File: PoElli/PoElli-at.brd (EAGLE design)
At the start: 100 x 80 mm, 142 parts, among them J1 DF12-ELLI-HEADER-TOP, J3 M022.54MM, J4 M022.54MM, Q1 SI1307DL, Q2 FDV301N, Q3 FDMC2674, Q4 IRFL4310, T1 Coilcraft 230NL, T2 FLYBACK750311689, U2 NCP1117, U3 FST3257, U4 LT3748, U5 TPS2378, U6 ENC424J600, X1 M-BOLT-2, X2 M-BOLT-2, X3 M-BOLT-2, X4 M-BOLT-2, Y1 25 MHz

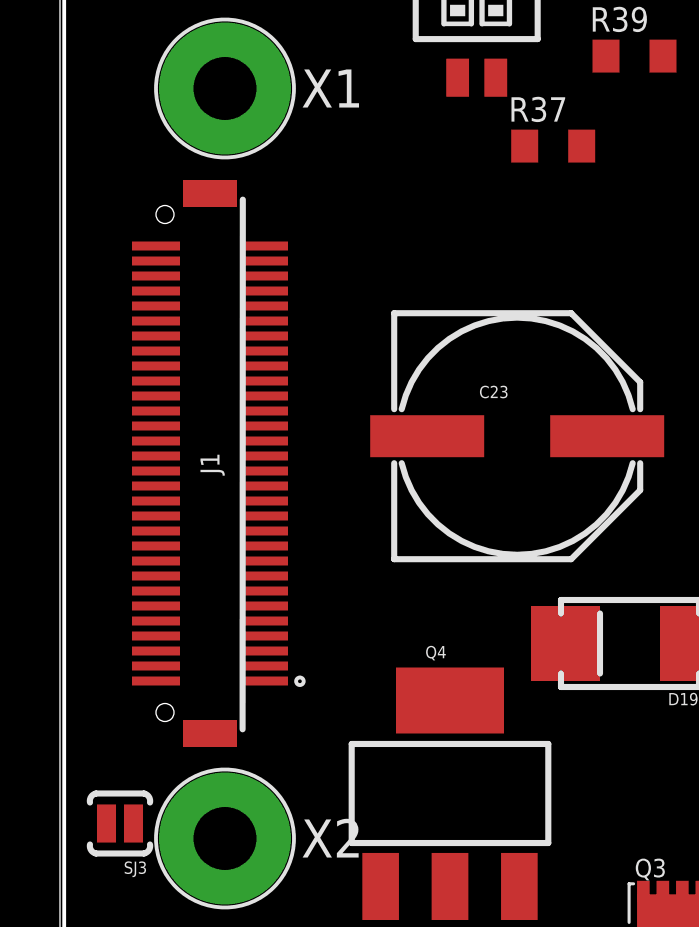
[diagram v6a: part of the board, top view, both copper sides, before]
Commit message: Move Hirose DF12 locations as agreed yesterday
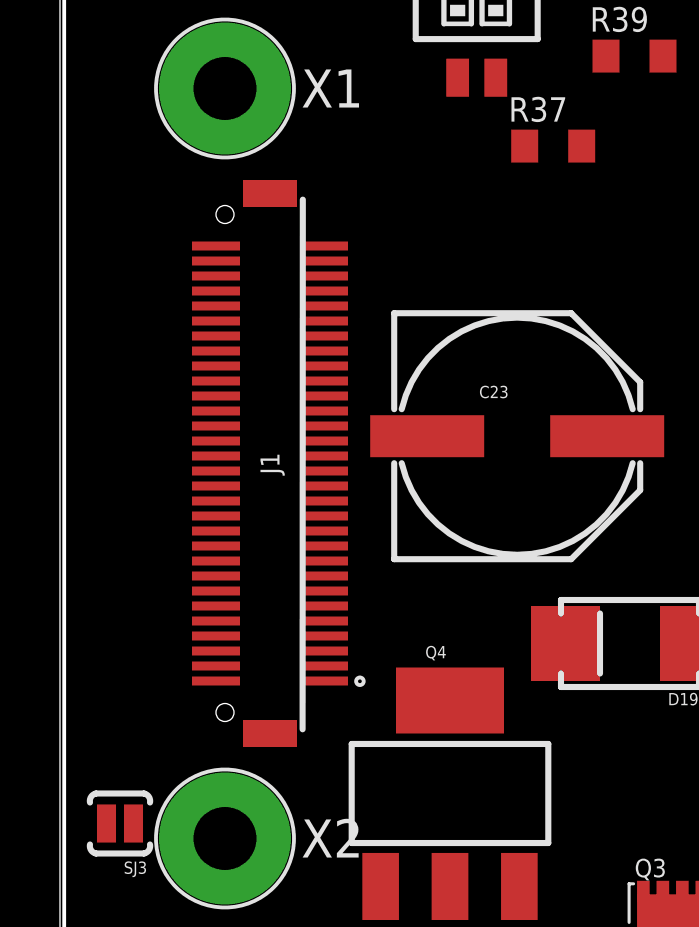
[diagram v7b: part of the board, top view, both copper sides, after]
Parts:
- moved J1 2.00 mm to (7.00, 28.0)
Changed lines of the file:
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@@
 <element name="C21" library="ELL-i-Passives" package="C0805" value="100nF" x="57.25" y="21.42"/>
 <element name="U2" library="ELL-i-PowerIC" package="SOT223" value="NCP1117" x="27.12" y="40.08"/>
-<element name="J1" library="ELL-i-Connectors" package="DF12(4.0)-60DP-0.5V" value="DF12-ELLI-HEADER-TOP" x="5" y="28" rot="R90"/>
+<element name="J1" library="ELL-i-Connectors" package="DF12(4.0)-60DP-0.5V" value="DF12-ELLI-HEADER-TOP" x="7" y="28" rot="R90"/>
 <element name="D17" library="ELL-i-DIscreteSemi" package="DIODE-B2100" value="B2100" x="57.8" y="42.31" rot="MR0"/>
 <element name="D16" library="ELL-i-DIscreteSemi" package="DIODE-B2100" value="B2100" x="57.68" y="33.81" rot="MR0"/>
@@
 <wire x1="18.24" y1="28.91" x2="22.8217" y2="23.9" width="0" layer="19" extent="1-1"/>
 <wire x1="29.4314" y1="36.9812" x2="18.24" y2="28.91" width="0" layer="19" extent="1-1"/>
-<wire x1="3.1999" y1="22.25" x2="18.24" y2="28.91" width="0" layer="19" extent="1-1"/>
+<wire x1="5.1999" y1="22.25" x2="18.24" y2="28.91" width="0" layer="19" extent="1-1"/>
 <wire x1="5.5" y1="40.5" x2="18.24" y2="28.91" width="0" layer="19" extent="1-1"/>
 <wire x1="5.08" y1="53.34" x2="5.5" y2="40.5" width="0" layer="19" extent="1-1"/>
@@
 <wire x1="22" y1="3.95" x2="25" y2="3.95" width="0" layer="19" extent="1-1"/>
 <wire x1="19" y1="3.95" x2="22" y2="3.95" width="0" layer="19" extent="1-1"/>
-<wire x1="3.1999" y1="31.75" x2="2.57" y2="44.8" width="0" layer="19" extent="1-1"/>
-<wire x1="3.1999" y1="23.75" x2="3.1999" y2="31.75" width="0" layer="19" extent="1-1"/>
-<wire x1="3.1999" y1="23.25" x2="3.1999" y2="23.75" width="0" layer="19" extent="1-1"/>
-<wire x1="5.5" y1="15.5" x2="3.1999" y2="23.25" width="0" layer="19" extent="1-1"/>
-<wire x1="12.24" y1="28.91" x2="3.1999" y2="31.75" width="0" layer="19" extent="1-1"/>
+<wire x1="5.1999" y1="31.75" x2="2.57" y2="44.8" width="0" layer="19" extent="1-1"/>
+<wire x1="5.1999" y1="23.75" x2="5.1999" y2="31.75" width="0" layer="19" extent="1-1"/>
+<wire x1="5.1999" y1="23.25" x2="5.1999" y2="23.75" width="0" layer="19" extent="1-1"/>
+<wire x1="5.5" y1="15.5" x2="5.1999" y2="23.25" width="0" layer="19" extent="1-1"/>
+<wire x1="12.24" y1="28.91" x2="5.1999" y2="31.75" width="0" layer="19" extent="1-1"/>
 <wire x1="71.61" y1="27.37" x2="68.24" y2="45.115" width="0" layer="19" extent="1-1"/>
 <wire x1="71.61" y1="24.89" x2="71.61" y2="27.37" width="0" layer="19" extent="1-1"/>
@@
 <wire x1="53.28" y1="72.14" x2="58.04" y2="73.34" width="0" layer="19" extent="1-1"/>
 <wire x1="54.955" y1="69.39" x2="53.28" y2="72.14" width="0" layer="19" extent="1-1"/>
-<wire x1="3.1999" y1="30.75" x2="54.955" y2="69.39" width="0" layer="19" extent="1-1"/>
+<wire x1="5.1999" y1="30.75" x2="54.955" y2="69.39" width="0" layer="19" extent="1-1"/>
 </signal>
 <signal name="TX+">
@@
 <contactref element="R39" pad="1"/>
 <wire x1="18.2" y1="41.58" x2="67.88" y2="71.29" width="0" layer="19" extent="1-1"/>
-<wire x1="3.1999" y1="28.75" x2="18.2" y2="41.58" width="0" layer="19" extent="1-1"/>
+<wire x1="5.1999" y1="28.75" x2="18.2" y2="41.58" width="0" layer="19" extent="1-1"/>
 </signal>
 <signal name="TX-">
@@
 <contactref element="J1" pad="36"/>
 <wire x1="15.49" y1="38.58" x2="67.88" y2="75.19" width="0" layer="19" extent="1-1"/>
-<wire x1="3.1999" y1="29.25" x2="15.49" y2="38.58" width="0" layer="19" extent="1-1"/>
+<wire x1="5.1999" y1="29.25" x2="15.49" y2="38.58" width="0" layer="19" extent="1-1"/>
 </signal>
 <signal name="RX+">
 <contactref element="U3" pad="5"/>
 <contactref element="J1" pad="38"/>
-<wire x1="3.1999" y1="29.75" x2="73.48" y2="73.89" width="0" layer="19" extent="1-1"/>
+<wire x1="5.1999" y1="29.75" x2="73.48" y2="73.89" width="0" layer="19" extent="1-1"/>
 </signal>
 <signal name="RX-">
 <contactref element="U3" pad="2"/>
 <contactref element="J1" pad="40"/>
-<wire x1="3.1999" y1="30.25" x2="73.48" y2="69.99" width="0" layer="19" extent="1-1"/>
+<wire x1="5.1999" y1="30.25" x2="73.48" y2="69.99" width="0" layer="19" extent="1-1"/>
 </signal>
 <signal name="N$40">
@@
 <wire x1="27.12" y1="36.9812" x2="27.12" y2="43.179" width="0" layer="19" extent="1-1"/>
 <wire x1="25.6" y1="33" x2="27.12" y2="36.9812" width="0" layer="19" extent="1-1"/>
-<wire x1="3.1999" y1="32.25" x2="25.6" y2="33" width="0" layer="19" extent="1-1"/>
-<wire x1="3.1999" y1="21.75" x2="3.1999" y2="32.25" width="0" layer="19" extent="1-1"/>
-<wire x1="1.55" y1="16" x2="3.1999" y2="21.75" width="0" layer="19" extent="1-1"/>
+<wire x1="5.1999" y1="32.25" x2="25.6" y2="33" width="0" layer="19" extent="1-1"/>
+<wire x1="5.1999" y1="21.75" x2="5.1999" y2="32.25" width="0" layer="19" extent="1-1"/>
+<wire x1="1.55" y1="16" x2="5.1999" y2="21.75" width="0" layer="19" extent="1-1"/>
 </signal>
 <signal name="ETH_INT">
@@
 <wire x1="19.72" y1="58.64" x2="15.3" y2="75.07" width="0" layer="19" extent="1-1"/>
 <wire x1="30.48" y1="50.8" x2="19.72" y2="58.64" width="0" layer="19" extent="1-1"/>
-<wire x1="3.1999" y1="33.75" x2="19.72" y2="58.64" width="0" layer="19" extent="1-1"/>
+<wire x1="5.1999" y1="33.75" x2="19.72" y2="58.64" width="0" layer="19" extent="1-1"/>
 </signal>
 <signal name="ETH_MISO">
@@
 <wire x1="33.82" y1="57.99" x2="15.3" y2="76.67" width="0" layer="19" extent="1-1"/>
 <wire x1="27.94" y1="50.8" x2="33.82" y2="57.99" width="0" layer="19" extent="1-1"/>
-<wire x1="3.1999" y1="34.25" x2="27.94" y2="50.8" width="0" layer="19" extent="1-1"/>
+<wire x1="5.1999" y1="34.25" x2="27.94" y2="50.8" width="0" layer="19" extent="1-1"/>
 </signal>
 <signal name="ETH_MOSI">
@@
 <wire x1="3.94" y1="58.64" x2="15.3" y2="75.87" width="0" layer="19" extent="1-1"/>
 <wire x1="25.4" y1="50.8" x2="3.94" y2="58.64" width="0" layer="19" extent="1-1"/>
-<wire x1="3.1999" y1="34.75" x2="3.94" y2="58.64" width="0" layer="19" extent="1-1"/>
+<wire x1="5.1999" y1="34.75" x2="3.94" y2="58.64" width="0" layer="19" extent="1-1"/>
 </signal>
 <signal name="N$72">
 <contactref element="J1" pad="57"/>
 <contactref element="SV1" pad="3"/>
-<wire x1="6.8001" y1="34.75" x2="5.08" y2="50.8" width="0" layer="19" extent="1-1"/>
+<wire x1="8.8001" y1="34.75" x2="5.08" y2="50.8" width="0" layer="19" extent="1-1"/>
 </signal>
 <signal name="N$73">
 <contactref element="SV1" pad="5"/>
 <contactref element="J1" pad="59"/>
-<wire x1="6.8001" y1="35.25" x2="7.62" y2="50.8" width="0" layer="19" extent="1-1"/>
+<wire x1="8.8001" y1="35.25" x2="7.62" y2="50.8" width="0" layer="19" extent="1-1"/>
 </signal>
 <signal name="N$74">
@@
 <contactref element="SW1" pad="1"/>
 <wire x1="13.255" y1="40.86" x2="30.48" y2="53.34" width="0" layer="19" extent="1-1"/>
-<wire x1="3.1999" y1="35.25" x2="13.255" y2="40.86" width="0" layer="19" extent="1-1"/>
+<wire x1="5.1999" y1="35.25" x2="13.255" y2="40.86" width="0" layer="19" extent="1-1"/>
 </signal>
 <signal name="ETH_SS">
@@
 <contactref element="J1" pad="2"/>
 <contactref element="SJ3" pad="1"/>
-<wire x1="2.45" y1="16" x2="3.1999" y2="20.75" width="0" layer="19" extent="1-1"/>
+<wire x1="2.45" y1="16" x2="5.1999" y2="20.75" width="0" layer="19" extent="1-1"/>
 </signal>
 </signals>

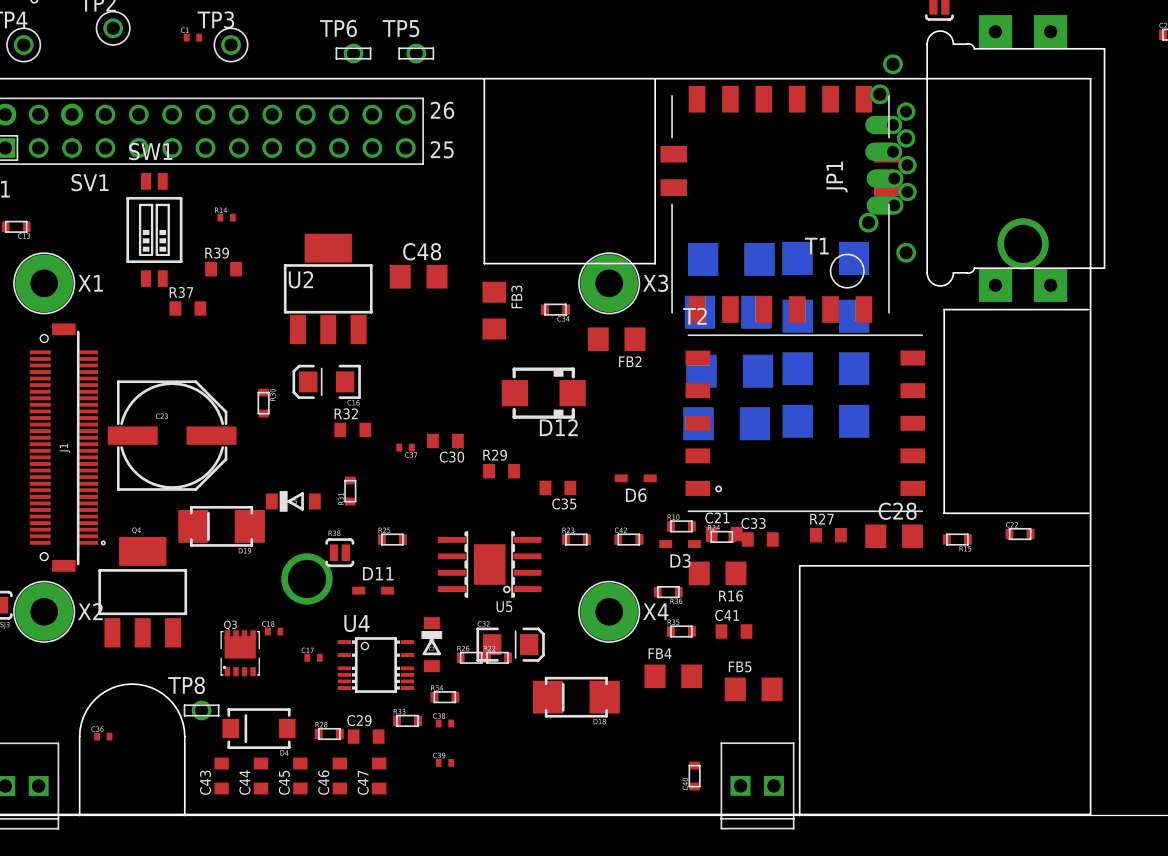
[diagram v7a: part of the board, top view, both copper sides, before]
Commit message: Update libraries on PoElli
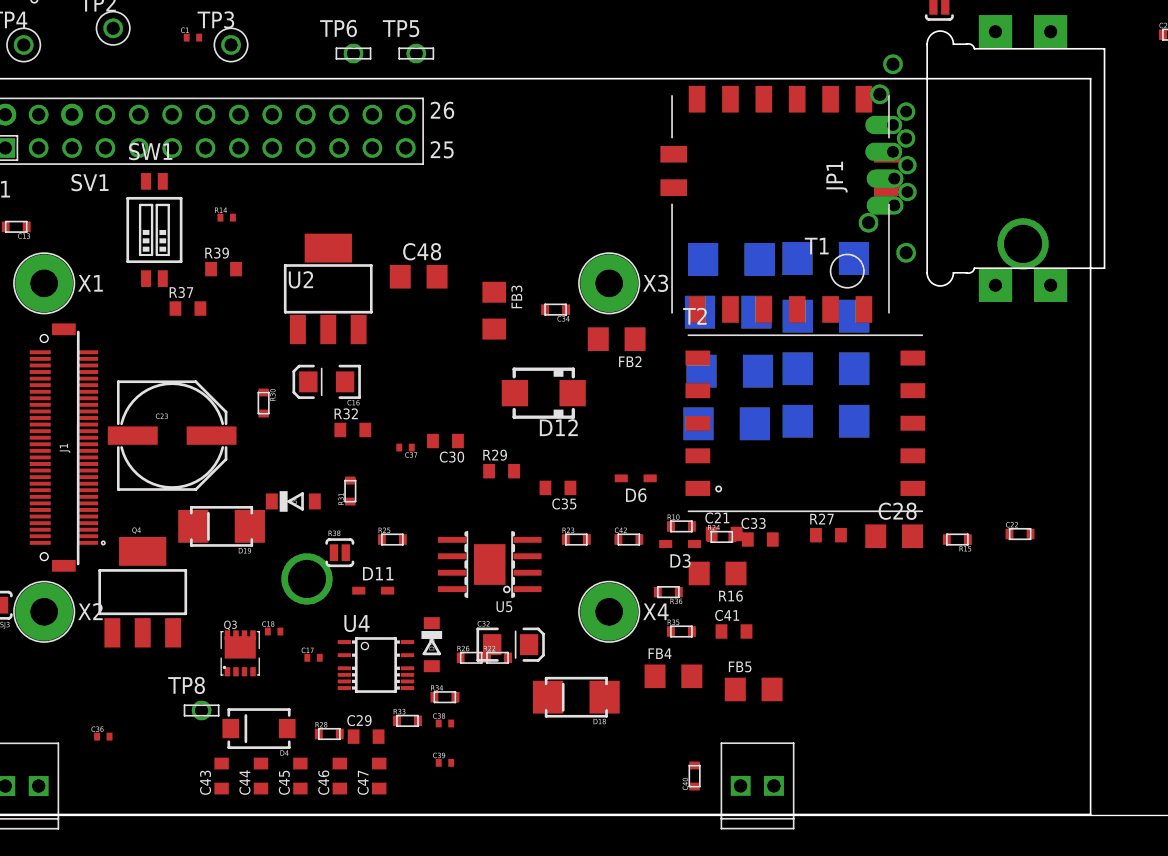
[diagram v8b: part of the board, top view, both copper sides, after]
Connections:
- new net 3.3V: SV1.1, SV1.17
- net RTN: no longer SV1.1, SV1.17
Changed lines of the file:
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@@
 <contactref element="C30" pad="2"/>
 <contactref element="D13" pad="A"/>
-<contactref element="SV1" pad="1"/>
-<contactref element="SV1" pad="17"/>
 <contactref element="R27" pad="2"/>
 <contactref element="C28" pad="1"/>
@@
 <wire x1="2.45" y1="16" x2="5.1999" y2="20.75" width="0" layer="19" extent="1-1"/>
 </signal>
+<signal name="3.3V">
+<contactref element="SV1" pad="1"/>
+<contactref element="SV1" pad="17"/>
+<wire x1="2.54" y1="50.8" x2="22.86" y2="50.8" width="0" layer="19" extent="1-1"/>
+</signal>
 </signals>
